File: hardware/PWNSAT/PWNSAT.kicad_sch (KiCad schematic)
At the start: 0 parts

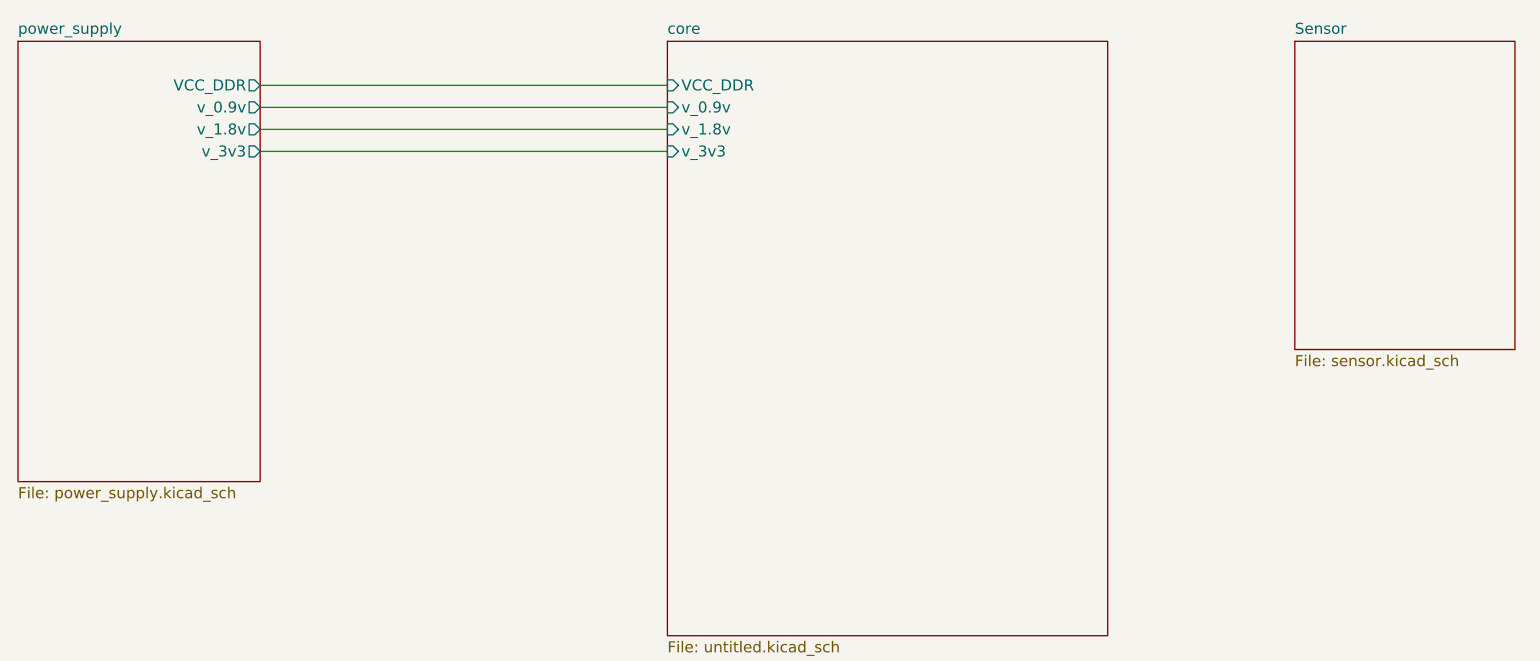
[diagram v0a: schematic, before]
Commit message: Feat(hw):Added_LoRa_module
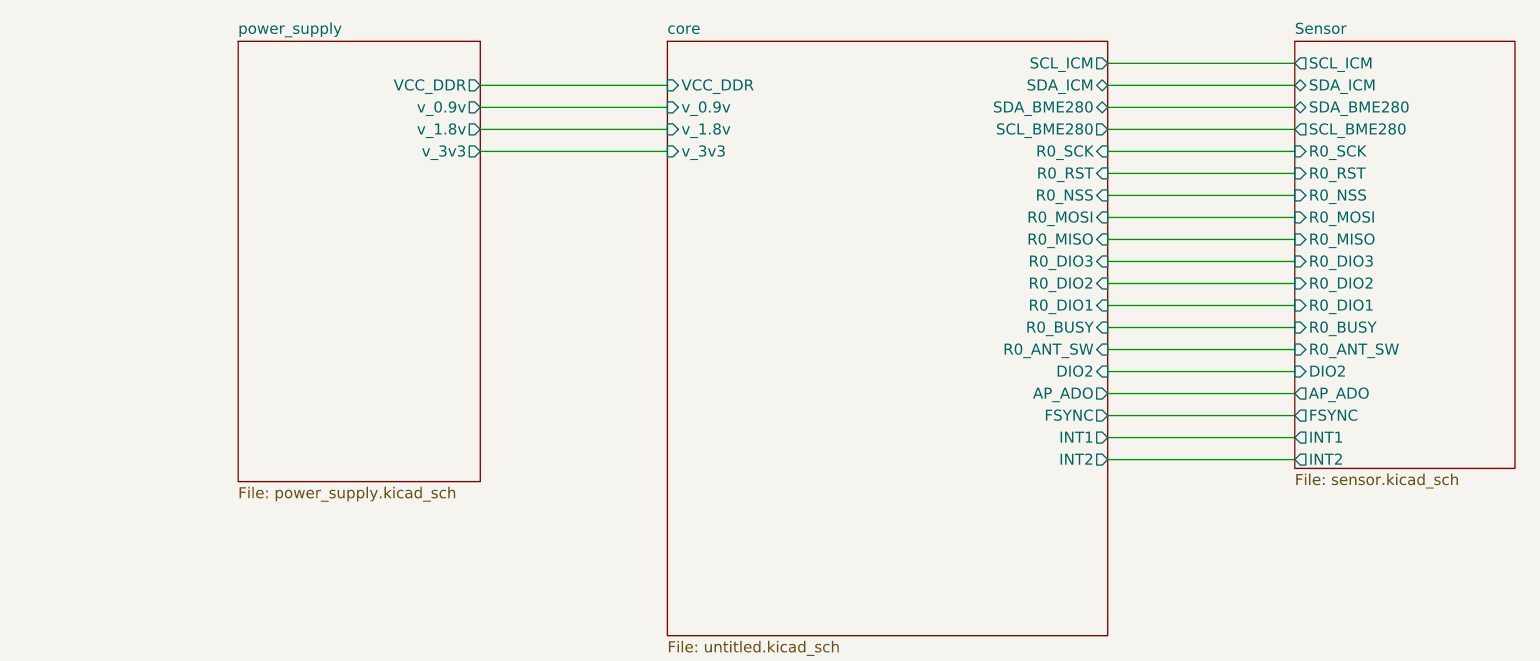
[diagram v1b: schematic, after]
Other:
- sheet Sensor ports: added AP_ADO, DIO2, FSYNC, INT1, INT2, R0_ANT_SW, R0_BUSY, R0_DIO1, R0_DIO2, R0_DIO3, R0_MISO, R0_MOSI, R0_NSS, R0_RST, R0_SCK, SCL_BME280, SCL_ICM, SDA_BME280, SDA_ICM; removed none
- sheet core ports: added AP_ADO, DIO2, FSYNC, INT1, INT2, R0_ANT_SW, R0_BUSY, R0_DIO1, R0_DIO2, R0_DIO3, R0_MISO, R0_MOSI, R0_NSS, R0_RST, R0_SCK, SCL_BME280, SCL_ICM, SDA_BME280, SDA_ICM; removed none

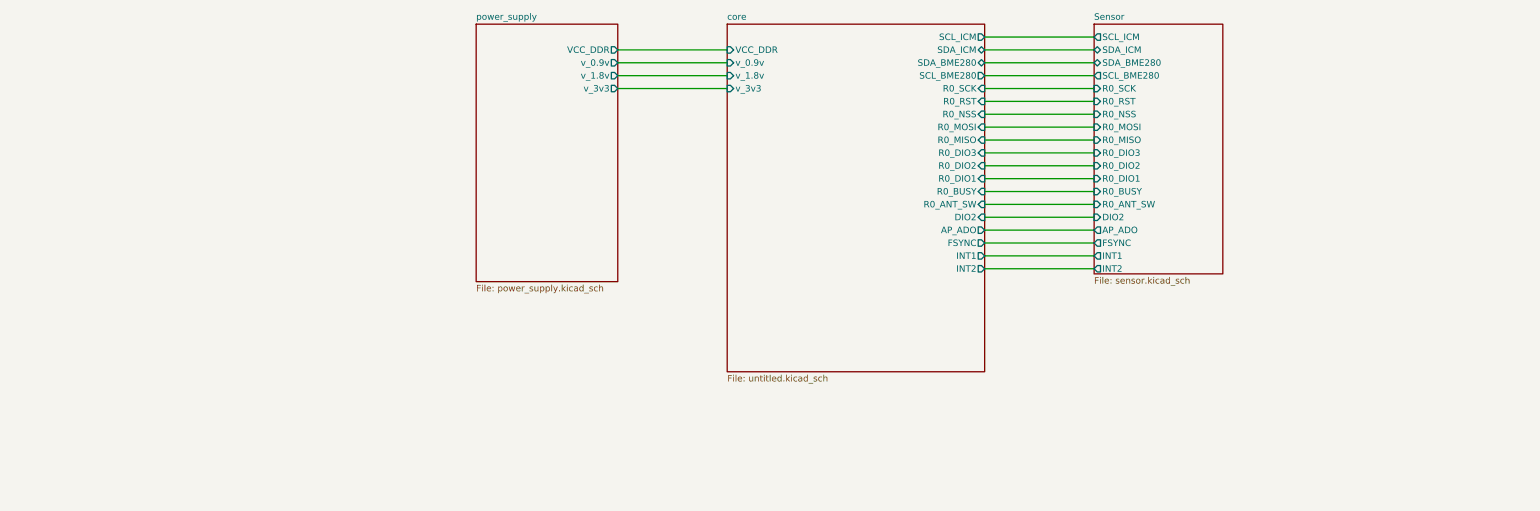
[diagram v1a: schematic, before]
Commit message: feat(Hw):Sch_Updated
Pending_Sensor_Connector
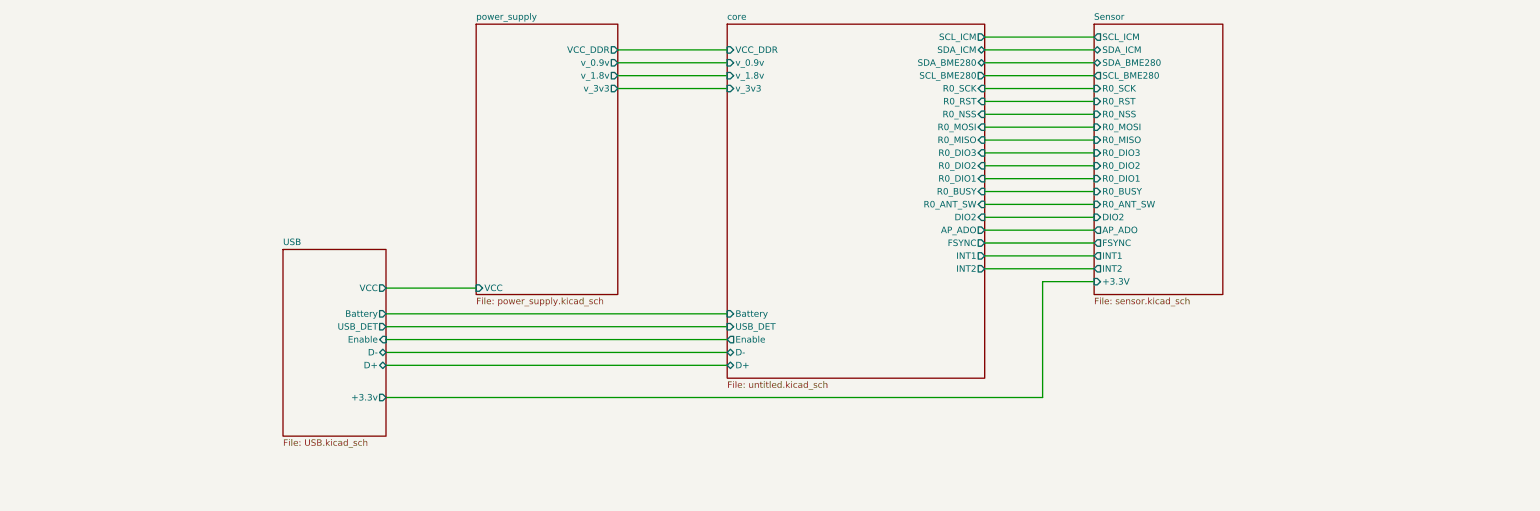
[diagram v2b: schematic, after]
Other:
- added sheet USB (USB.kicad_sch)
- sheet Sensor ports: added +3.3V; removed none
- sheet core ports: added Battery, D+, D-, Enable, USB_DET; removed none
- sheet power_supply ports: added VCC; removed none
- company: (none) -> Electronic Cats
- title: (none) -> Cube_Sat

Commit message: feat(Hw):Battery_Board_pro_Updated
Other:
- sheet USB renamed Source_Connector
- added sheet USB_Selector (USB_Selector.kicad_sch)
- sheet Source_Connector: file USB.kicad_sch -> Source_Connector.kicad_sch
- sheet Source_Connector ports: added 2_DN, 2_DP; removed +3.3v, D+, D-

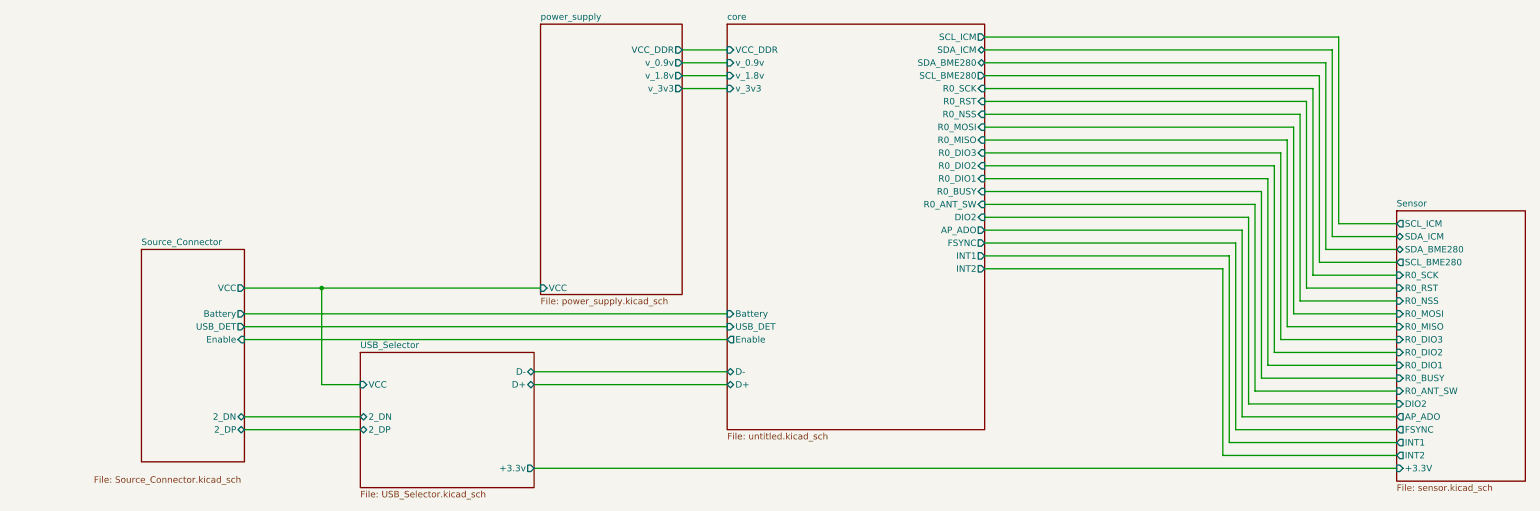
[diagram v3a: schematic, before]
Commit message: feat(Hw):Update_Battery_Sch_And_Sensors_And_PWNCube
pending_Outputs_connectors
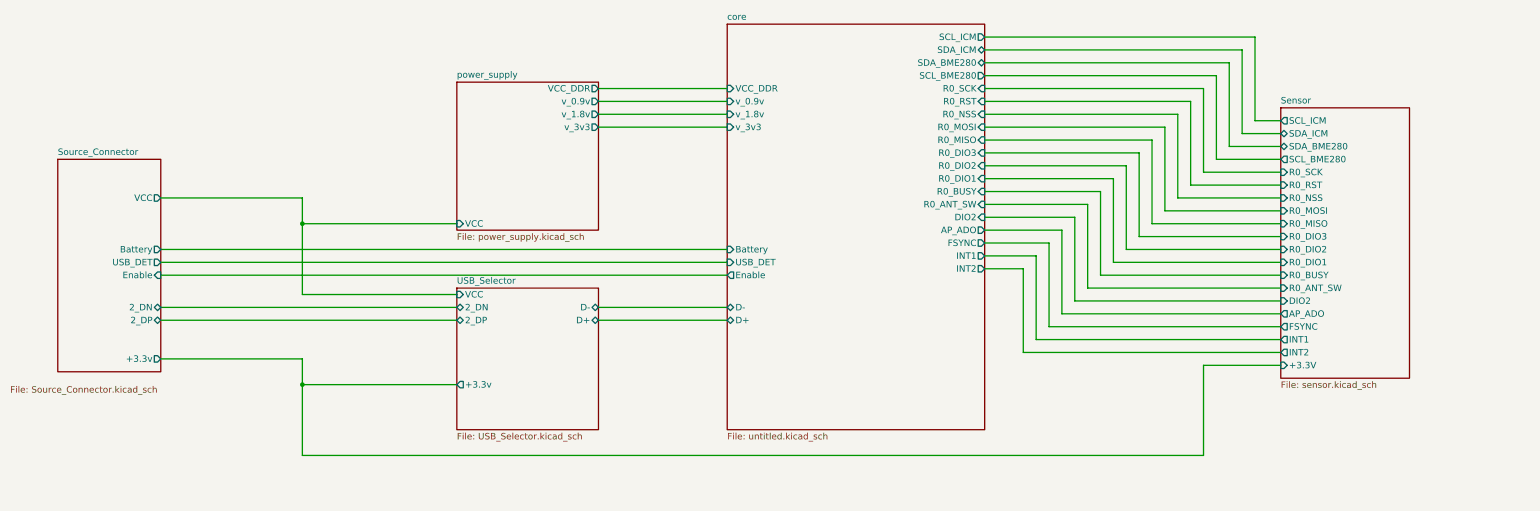
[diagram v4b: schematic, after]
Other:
- sheet Source_Connector ports: added +3.3v; removed none

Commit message: feat(Hw):floorplans_updated
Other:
- sheet Sensor ports: added DIO23, R1_ANT_SW, R1_BUSY, R1_DIO1, R1_DIO2, R1_DIO3, R1_MISO, R1_MOSI, R1_NSS, R1_RST, R1_SCK; removed none
- sheet core ports: added DIO23, R1_ANT_SW, R1_BUSY, R1_DIO1, R1_DIO2, R1_DIO3, R1_MISO, R1_MOSI, R1_NSS, R1_RST, R1_SCK; removed none

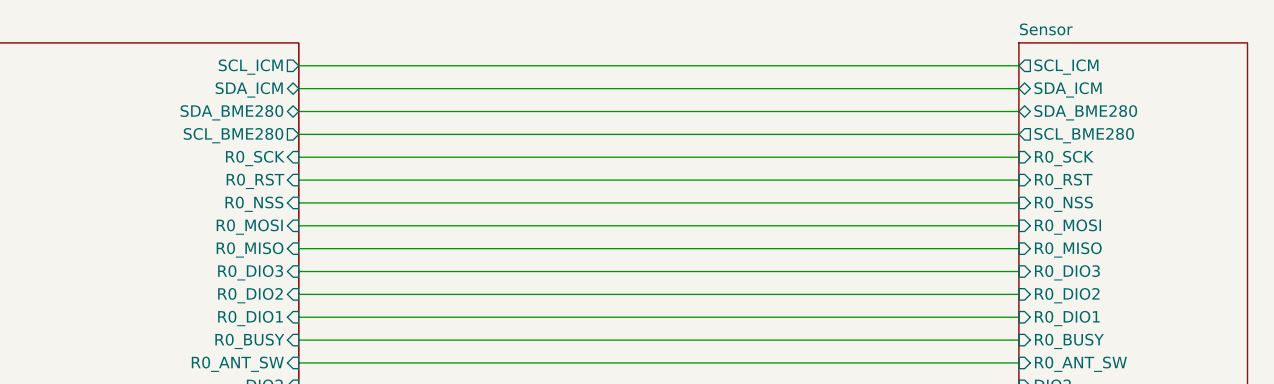
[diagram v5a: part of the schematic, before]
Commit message: feat(Hw):Boards_Updated
Pending_Sensors_Board
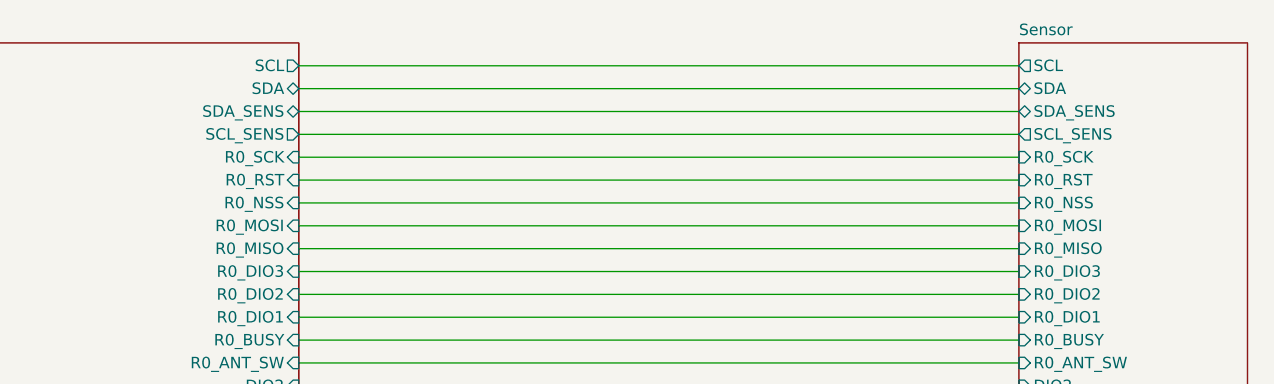
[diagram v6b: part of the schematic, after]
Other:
- sheet Sensor ports: added SCL, SCL_SENS, SDA, SDA_SENS; removed SCL_BME280, SCL_ICM, SDA_BME280, SDA_ICM
- sheet core ports: added SCL, SCL_SENS, SDA, SDA_SENS; removed SCL_BME280, SCL_ICM, SDA_BME280, SDA_ICM
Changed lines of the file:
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@@
-			)
-		)
-		(pin "SCL_BME280" output
-			(at 278.13 111.76 180)
-			(effects
-				(font
-					(size 1.27 1.27)
-				)
-				(justify left)
 			)
 		)
@@
 			)
 		)
-		(pin "SDA_ICM" bidirectional
-			(at 278.13 106.68 180)
-			(effects
-				(font
-					(size 1.27 1.27)
-				)
-				(justify left)
-			)
-		)
 		(pin "R0_RST" input
 			(at 278.13 116.84 180)
@@
 			)
 		)
-		(pin "SCL_ICM" output
-			(at 278.13 104.14 180)
-			(effects
-				(font
-					(size 1.27 1.27)
-				)
-				(justify left)
-			)
-		)
 		(pin "R0_DIO1" input
 			(at 278.13 132.08 180)
@@
 			)
 		)
-		(pin "SDA_BME280" bidirectional
-			(at 278.13 109.22 180)
-			(effects
-				(font
-					(size 1.27 1.27)
-				)
-				(justify left)
-			)
-		)
 		(pin "FSYNC" output
 			(at 278.13 144.78 180)
@@
 		(pin "R1_RST" input
 			(at 278.13 179.07 180)
+			(effects
+				(font
+					(size 1.27 1.27)
+				)
+				(justify left)
+			)
+		)
+		(pin "SDA" bidirectional
+			(at 278.13 106.68 180)
+			(effects
+				(font
+					(size 1.27 1.27)
+				)
+				(justify left)
+			)
+		)
+		(pin "SDA_SENS" bidirectional
+			(at 278.13 109.22 180)
+			(effects
+				(font
+					(size 1.27 1.27)
+				)
+				(justify left)
+			)
+		)
+		(pin "SCL" output
+			(at 278.13 104.14 180)
+			(effects
+				(font
+					(size 1.27 1.27)
+				)
+				(justify left)
+			)
+		)
+		(pin "SCL_SENS" output
+			(at 278.13 111.76 180)
 			(effects
 				(font
@@
 			)
 		)
-		(pin "SCL_BME280" output
-			(at 198.12 111.76 0)
-			(effects
-				(font
-					(size 1.27 1.27)
-				)
-				(justify right)
-			)
-		)
-		(pin "SCL_ICM" output
-			(at 198.12 104.14 0)
-			(effects
-				(font
-					(size 1.27 1.27)
-				)
-				(justify right)
-			)
-		)
-		(pin "SDA_BME280" bidirectional
-			(at 198.12 109.22 0)
-			(effects
-				(font
-					(size 1.27 1.27)
-				)
-				(justify right)
-			)
-		)
-		(pin "SDA_ICM" bidirectional
-			(at 198.12 106.68 0)
-			(effects
-				(font
-					(size 1.27 1.27)
-				)
-				(justify right)
-			)
-		)
 		(pin "AP_ADO" output
 			(at 198.12 142.24 0)
@@
 			(effects
 				(font
+					(size 1.27 1.27)
+				)
+				(justify right)
+			)
+		)
+		(pin "SCL_SENS" output
+			(at 198.12 111.76 0)
+			(effects
+				(font
+					(size 1.27 1.27)
+				)
+				(justify right)
+			)
+		)
+		(pin "SDA" bidirectional
+			(at 198.12 106.68 0)
+			(effects
+				(font
+					(size 1.27 1.27)
+				)
+				(justify right)
+			)
+		)
+		(pin "SDA_SENS" bidirectional
+			(at 198.12 109.22 0)
+			(effects
+				(font
+					(size 1.27 1.27)
+				)
+				(justify right)
+			)
+		)
+		(pin "SCL" output
+			(at 198.12 104.14 0)
+			(effects
+				(font
